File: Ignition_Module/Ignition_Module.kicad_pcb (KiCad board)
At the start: 2 copper layers, 65 x 65 mm, 68 parts, among them J1 Conn_01x01_Pin, J10 Conn_01x01_Pin, J11 Conn_01x01_Pin, J12 Conn_01x01_Pin, J13 Conn_01x01_Pin, J14 Conn_01x01_Pin, J15 Conn_01x01_Pin, J16 Conn_01x01_Pin, J2 Conn_01x01_Pin, J3 Conn_01x01_Pin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

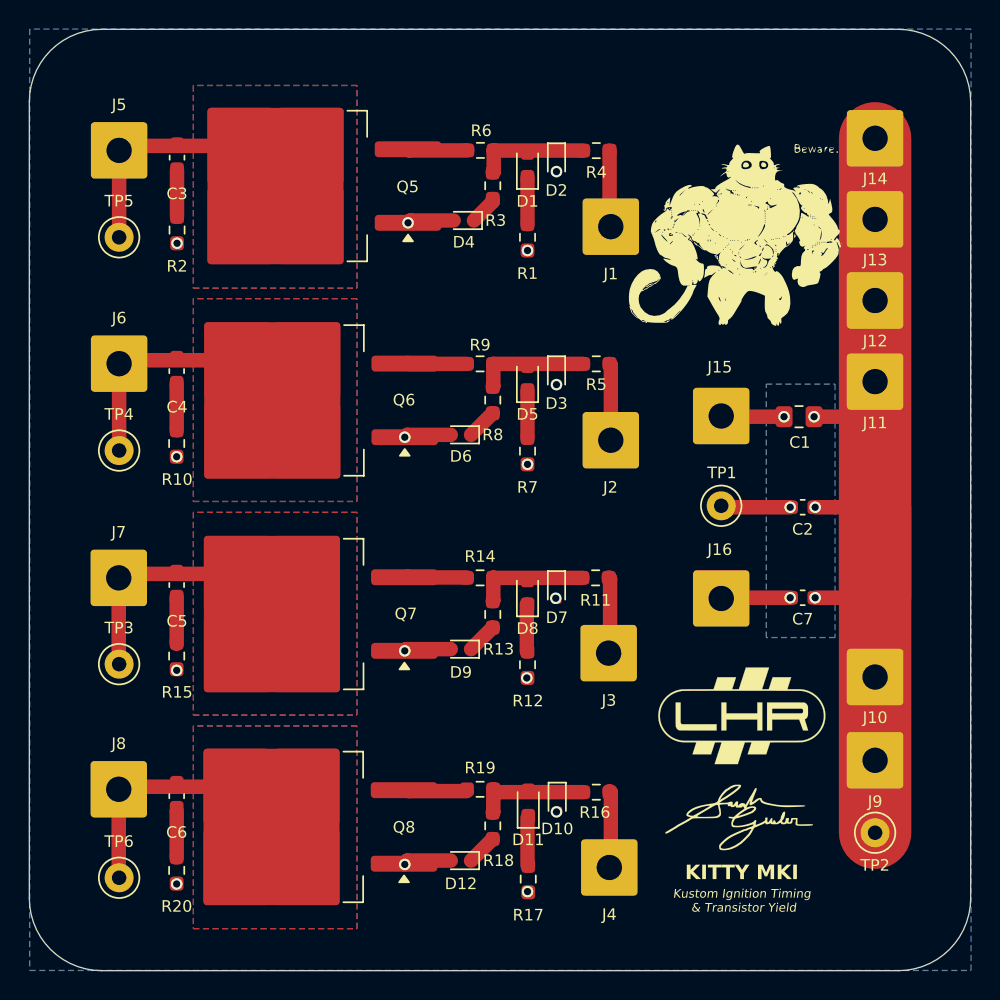
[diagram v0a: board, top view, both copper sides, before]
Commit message: added mounting holes + silkscreen
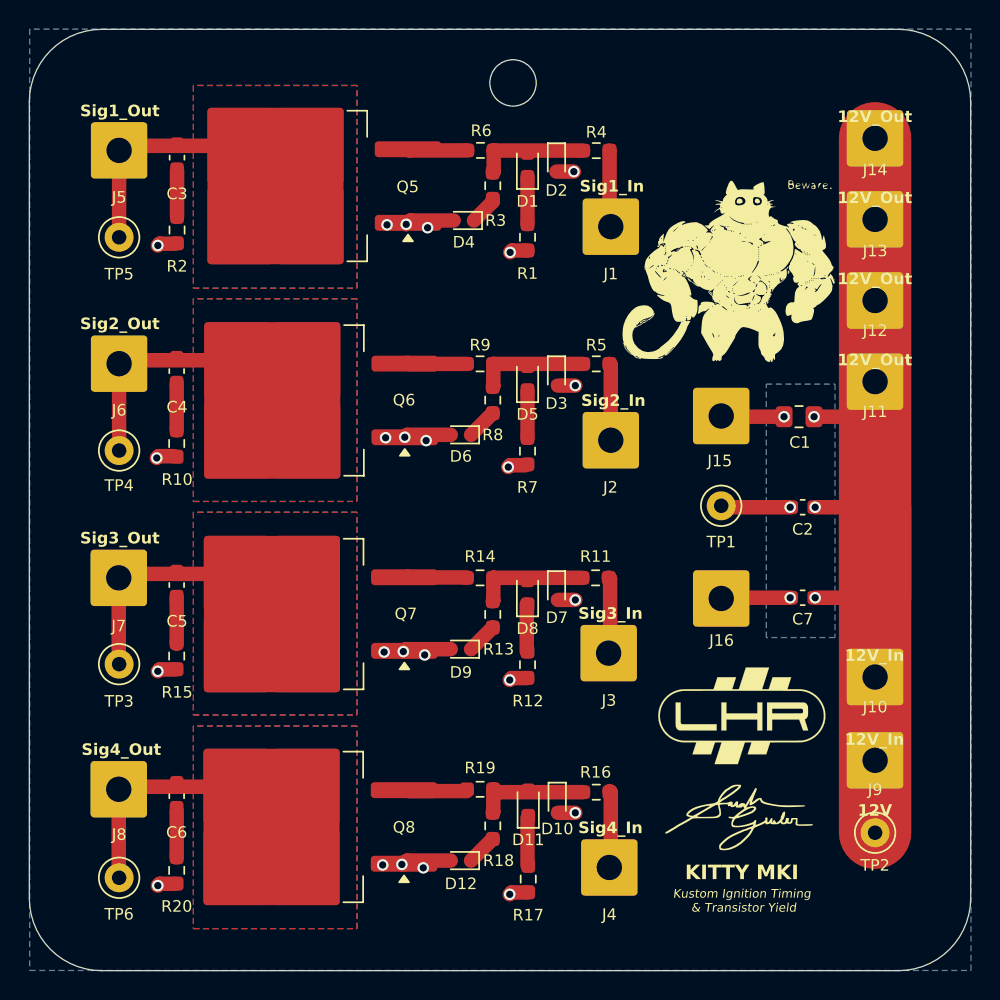
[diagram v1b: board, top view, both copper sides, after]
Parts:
- added REF**: MountingHole_3.2mm_M3, LHR:MountingHole_3.2mm_M3, F.Cu at (133.4, 83.7)
- moved G*** 2.54 mm to (149.0, 96.4)
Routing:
- net GND: track 27.3 -> 42.8 mm, vias 19 -> 27
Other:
- board text added: "12V"
- board text added: "12V_In"
- board text added: "12V_Out"
- board text added: "Sig1_In"
- board text added: "Sig1_Out"
- board text added: "Sig2_In"
- board text added: "Sig2_Out"
- board text added: "Sig3_In"
- board text added: "Sig3_Out"
- board text added: "Sig4_In"
- board text added: "Sig4_Out"

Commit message: removed diode - makes gate float 10V
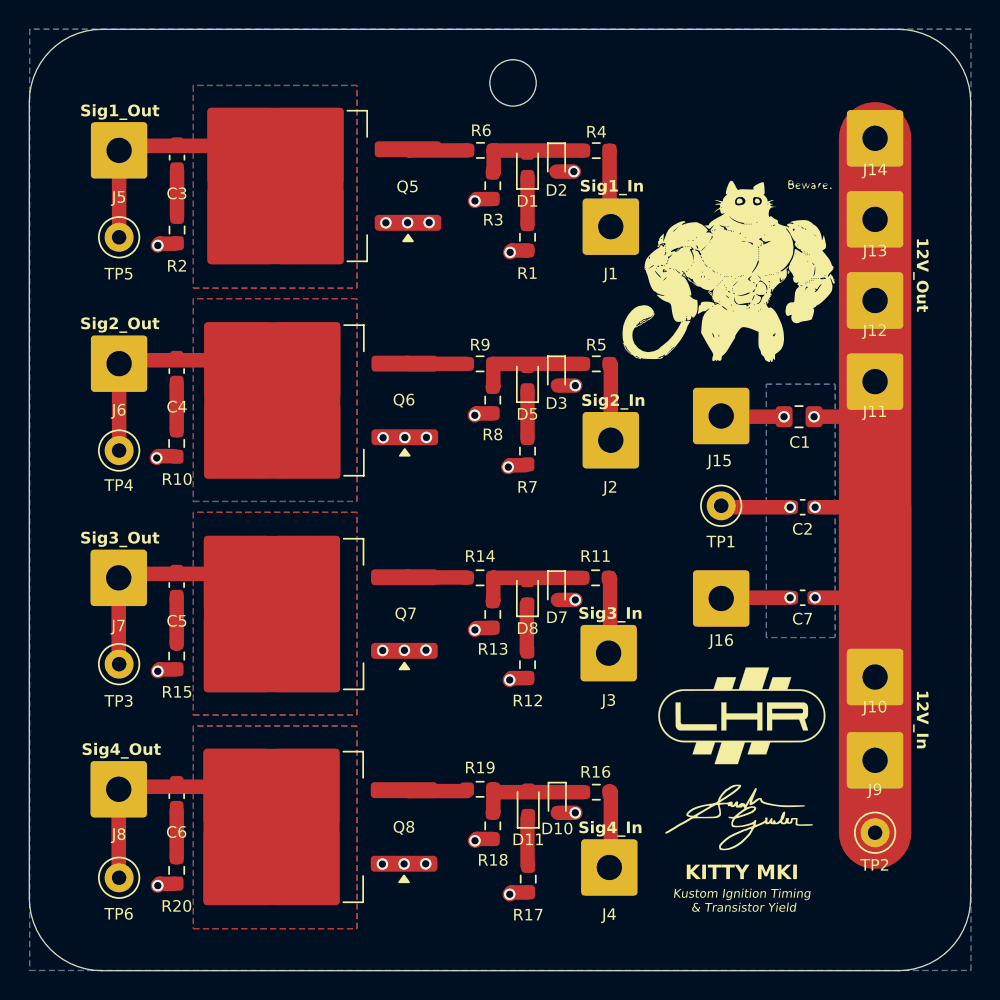
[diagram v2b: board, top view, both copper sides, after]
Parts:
- removed D12, D4, D6, D9: 10V, Diode_SMD:D_SOD-523
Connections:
- R13 pad 2: Net-(D9-K) -> GND
- R18 pad 2: Net-(D12-K) -> GND
- R3 pad 2: Net-(D4-K) -> GND
- R8 pad 2: Net-(D6-K) -> GND
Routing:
- net GND: track 42.8 -> 33.9 mm, vias 27 -> 31
- net Net-(D12-K): track 2.12 -> 0.00 mm
- net Net-(D9-K): track 2.12 -> 0.00 mm
- net Net-(D6-K): track 2.12 -> 0.00 mm
- net Net-(D4-K): track 2.03 -> 0.00 mm
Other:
- board text removed: "12V"

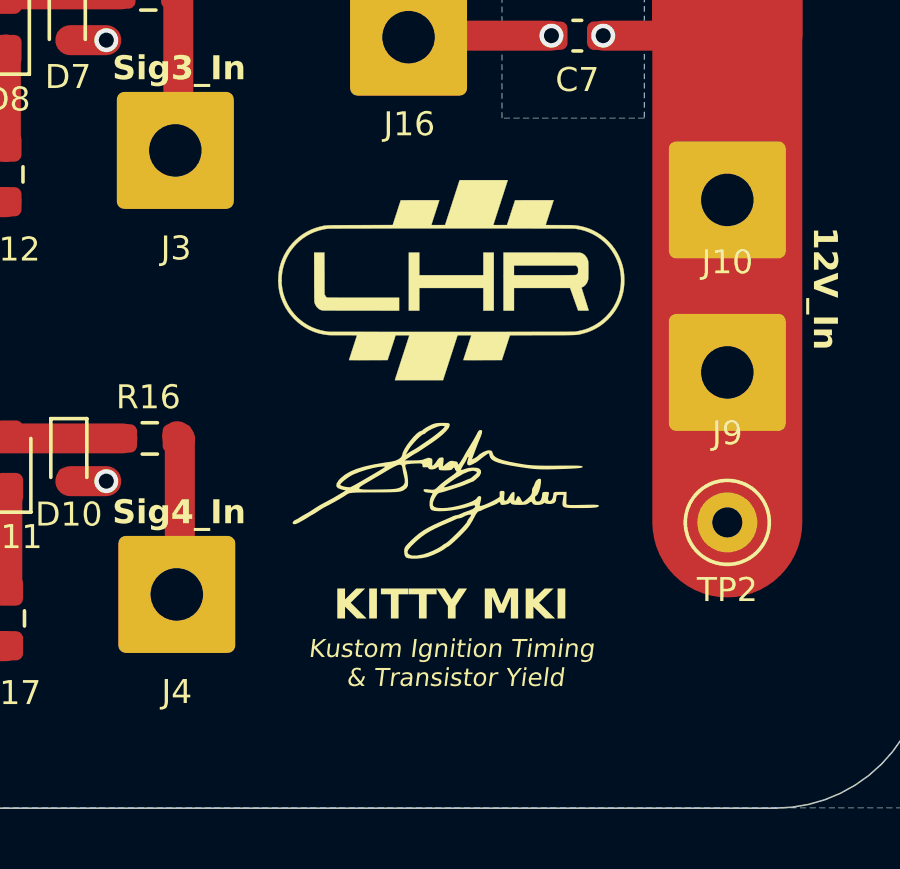
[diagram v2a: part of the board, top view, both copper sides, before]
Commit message: Added name and year
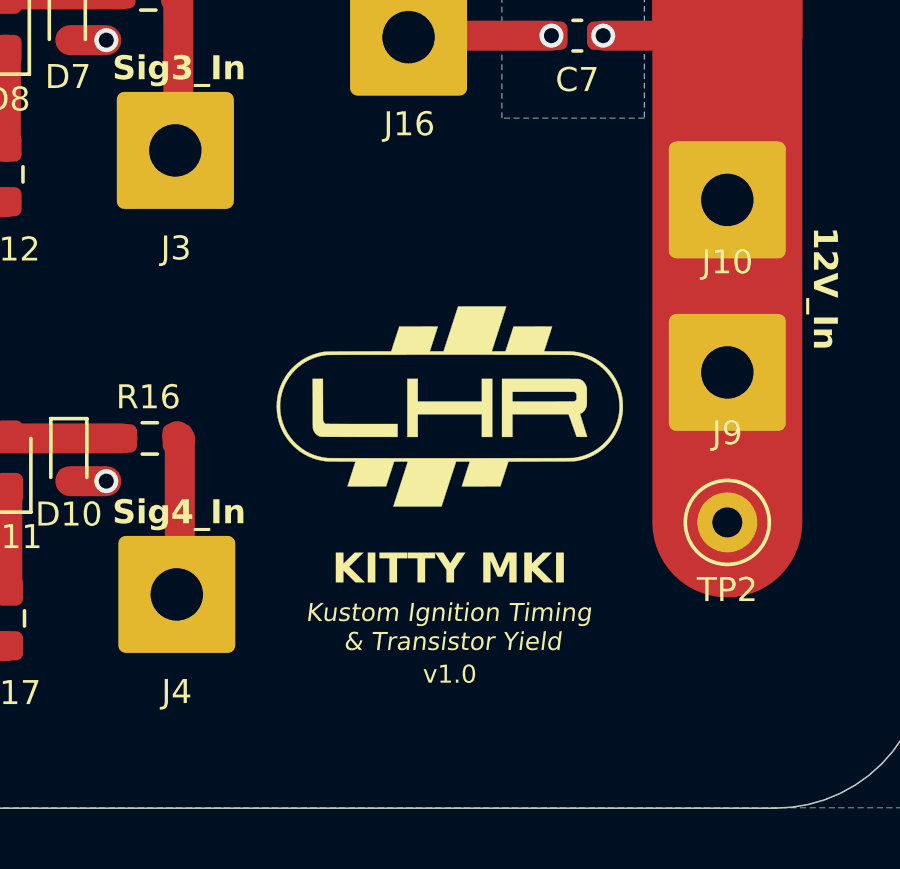
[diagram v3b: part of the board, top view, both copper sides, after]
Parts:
- G***: moved to B.Cu
- moved G*** 29.0 mm to (130.1, 112.2), turned to 180 degrees
- moved G*** 4.21 mm to (149.2, 131.6)
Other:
- board text added: "Sarah Gruber 2026"
- board text added: "v1.0"
